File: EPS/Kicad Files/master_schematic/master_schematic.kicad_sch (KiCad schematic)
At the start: 0 parts

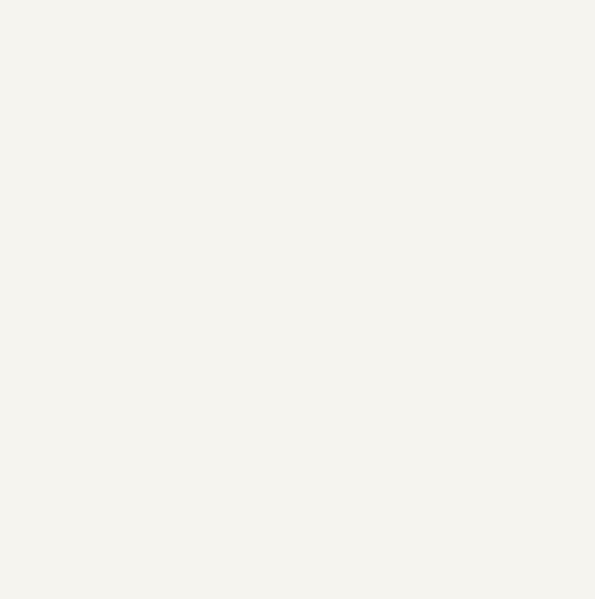
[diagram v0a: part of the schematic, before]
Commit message: Added MCU/CAN to master schematic
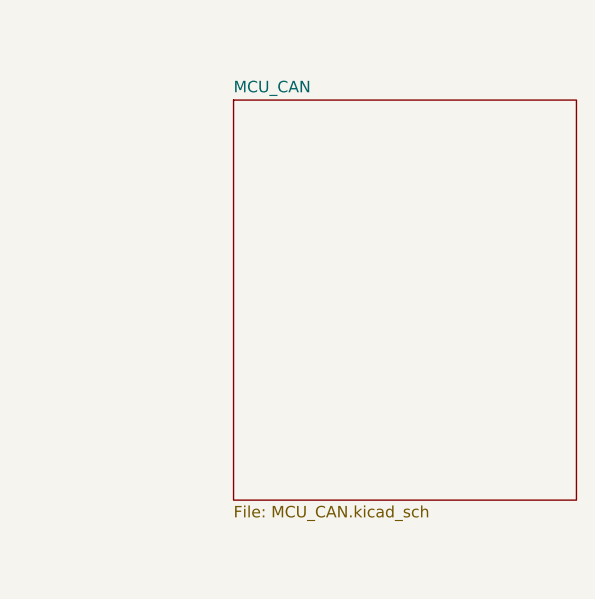
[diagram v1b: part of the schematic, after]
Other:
- added sheet MCU_CAN (MCU_CAN.kicad_sch)
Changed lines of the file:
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@@
+    )
+  )
+  (sheet (at 187.96 67.31) (size 38.1 44.45) (fields_autoplaced)
+    (stroke (width 0.1524) (type solid) (color 0 0 0 0))
+    (fill (color 0 0 0 0.0000))
+    (property "Sheet name" "MCU_CAN" (id 0) (at 187.96 66.5984 0)
+      (effects (font (size 1.27 1.27)) (justify left bottom))
+    )
+    (property "Sheet file" "MCU_CAN.kicad_sch" (id 1) (at 187.96 112.3446 0)
+      (effects (font (size 1.27 1.27)) (justify left top))
     )
   )
@@
     (path "/59a4dc33-016c-4cea-b648-6fe1c8836f68" (page "2"))
     (path "/26a06af6-a463-4c0b-bc99-b7ef2964e4cd" (page "3"))
+    (path "/9fdbccc2-2f8e-4736-8eda-6be5762e5cd4" (page "4"))
   )
   (symbol_instances
@@
       (reference "#PWR01") (unit 1) (value "GNDPWR") (footprint "")
     )
+    (path "/9fdbccc2-2f8e-4736-8eda-6be5762e5cd4/3b6c9550-f562-4564-bb93-fa871679251c"
+      (reference "#PWR0101") (unit 1) (value "+5V") (footprint "")
+    )
     (path "/26a06af6-a463-4c0b-bc99-b7ef2964e4cd/4d6c0c89-4050-4aad-865b-8bf0a01a4f8a"
       (reference "#PWR0101") (unit 1) (value "GND") (footprint "")
     )
+    (path "/9fdbccc2-2f8e-4736-8eda-6be5762e5cd4/5188dfb7-7eb6-4f46-9d1e-d138f6f4b6b9"
+      (reference "#PWR0102") (unit 1) (value "GND") (footprint "")
+    )
     (path "/26a06af6-a463-4c0b-bc99-b7ef2964e4cd/7e8ecf40-acc3-4991-b27f-c274de50e623"
       (reference "#PWR0102") (unit 1) (value "GNDPWR") (footprint "")
     )
+    (path "/9fdbccc2-2f8e-4736-8eda-6be5762e5cd4/938f820b-db08-4a16-82b8-08a6ddecc1d4"
+      (reference "#PWR0103") (unit 1) (value "GND") (footprint "")
+    )
+    (path "/9fdbccc2-2f8e-4736-8eda-6be5762e5cd4/8a5d2036-f5c8-4423-a580-7532d25abfcb"
+      (reference "#PWR0104") (unit 1) (value "+5V") (footprint "")
+    )
     (path "/26a06af6-a463-4c0b-bc99-b7ef2964e4cd/f10741fa-1902-4bc1-9462-3f90d5329911"
       (reference "#PWR0104") (unit 1) (value "GND") (footprint "")
@@
       (reference "#PWR?") (unit 1) (value "GND") (footprint "")
     )
+    (path "/9fdbccc2-2f8e-4736-8eda-6be5762e5cd4/68eca964-9fa2-4a67-b630-c953d1e85d42"
+      (reference "C1") (unit 1) (value "C") (footprint "")
+    )
     (path "/59a4dc33-016c-4cea-b648-6fe1c8836f68/9badf30d-e9b0-4bf0-8024-97ff6edd9f1c"
       (reference "C1") (unit 1) (value "20μF") (footprint "")
@@
       (reference "J1") (unit 1) (value "USB_C_Receptacle") (footprint "Connector_USB:USB_C_Receptacle_Amphenol_12401610E4-2A")
     )
+    (path "/9fdbccc2-2f8e-4736-8eda-6be5762e5cd4/99f4b5e6-a691-4fc9-af7d-e683f2ec248c"
+      (reference "JP1") (unit 1) (value "Jumper_2_Open") (footprint "")
+    )
     (path "/26a06af6-a463-4c0b-bc99-b7ef2964e4cd/3e50bbb4-8a65-44e5-81ec-f7ea9020e1e8"
       (reference "L1") (unit 1) (value ".47uH") (footprint "Inductor_SMD:L_1008_2520Metric")
@@
       (reference "R1") (unit 1) (value "1k") (footprint "Resistor_SMD:R_0402_1005Metric")
     )
+    (path "/9fdbccc2-2f8e-4736-8eda-6be5762e5cd4/ef997102-133d-40f7-998b-a781a8ae245c"
+      (reference "R1") (unit 1) (value "R") (footprint "")
+    )
     (path "/59a4dc33-016c-4cea-b648-6fe1c8836f68/0eedaf4c-41f6-48ba-98ff-d706984035d0"
       (reference "R2") (unit 1) (value "PSF4NTEBL500F") (footprint "footprints:PSF4NTEBL500F")
@@
       (reference "R2") (unit 1) (value "24.9k") (footprint "Resistor_SMD:R_0402_1005Metric")
     )
+    (path "/9fdbccc2-2f8e-4736-8eda-6be5762e5cd4/ff83ad68-5cb3-4e1d-bfd7-46775b78c1ac"
+      (reference "R2") (unit 1) (value "R") (footprint "")
+    )
     (path "/59a4dc33-016c-4cea-b648-6fe1c8836f68/40193638-446d-4ec3-b217-bab5b5e47e99"
       (reference "R3") (unit 1) (value "PSF4NTEBL500F") (footprint "footprints:PSF4NTEBL500F")
@@
       (reference "R3") (unit 1) (value "1k") (footprint "Resistor_SMD:R_0402_1005Metric")
     )
+    (path "/9fdbccc2-2f8e-4736-8eda-6be5762e5cd4/c035cb9d-aa77-4291-97bb-83d02bf9c2a0"
+      (reference "R3") (unit 1) (value "R") (footprint "")
+    )
+    (path "/9fdbccc2-2f8e-4736-8eda-6be5762e5cd4/146d4fbc-56d3-4fb3-82bd-259d588c93f2"
+      (reference "R4") (unit 1) (value "R") (footprint "")
+    )
     (path "/26a06af6-a463-4c0b-bc99-b7ef2964e4cd/7b1c5fbf-250a-41c6-a9a3-633299511edf"
       (reference "R4") (unit 1) (value "10k") (footprint "Resistor_SMD:R_0402_1005Metric")
@@
       (reference "U1") (unit 1) (value "RPM5.0-2.0") (footprint "Converter_DCDC:Converter_DCDC_RECOM_RPMx.x-x.0")
     )
+    (path "/9fdbccc2-2f8e-4736-8eda-6be5762e5cd4/694c3c7b-983e-4abf-8a12-4500e08a960e"
+      (reference "U1") (unit 1) (value "PIC18F27Q84-E/SP") (footprint "PIC18F27Q84-E-SP:PIC18F27Q84-E&slash_SP")
+    )
     (path "/26a06af6-a463-4c0b-bc99-b7ef2964e4cd/921339e0-e2c4-4bf6-a72a-ff2acad226de"
       (reference "U1") (unit 1) (value "MAX77757JEFG435+") (footprint "77757 foot:IC_MAX77757JEFG435+")
     )
+    (path "/9fdbccc2-2f8e-4736-8eda-6be5762e5cd4/1543425c-7d7b-48c0-9e08-4616ac873bc9"
+      (reference "U2") (unit 1) (value "ATA6560-GAQW-VAO") (footprint "ATA6560-GAQW-VAO:ATA6560-GAQW-VAO")
+    )
     (path "/26a06af6-a463-4c0b-bc99-b7ef2964e4cd/62903ce9-1929-4ae0-8378-6aa7c4209eef"

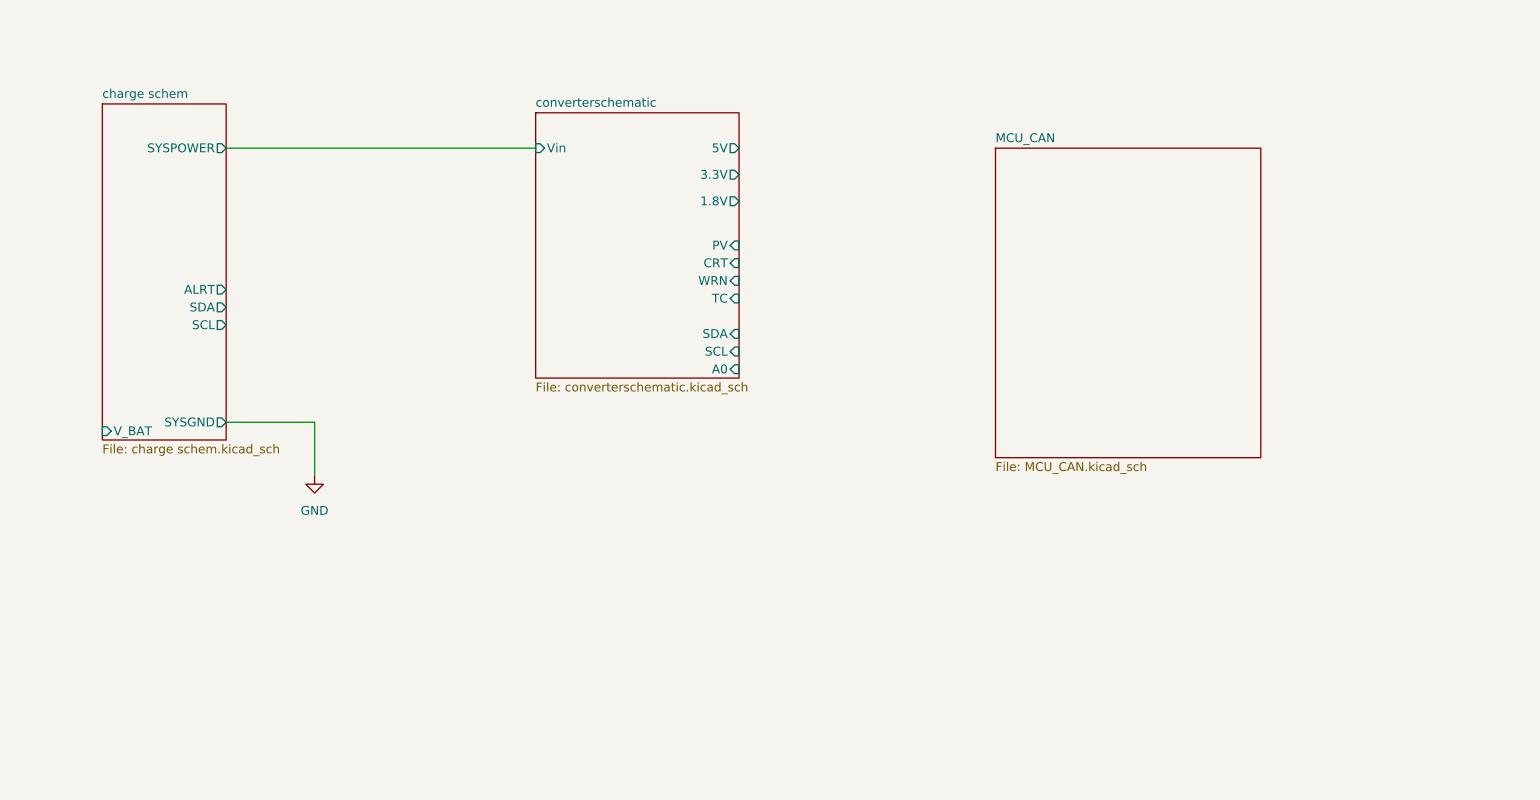
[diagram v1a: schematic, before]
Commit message: master schematic update
added hierarchal pins to MCU_CAN, and attached it with the rest of the circuit
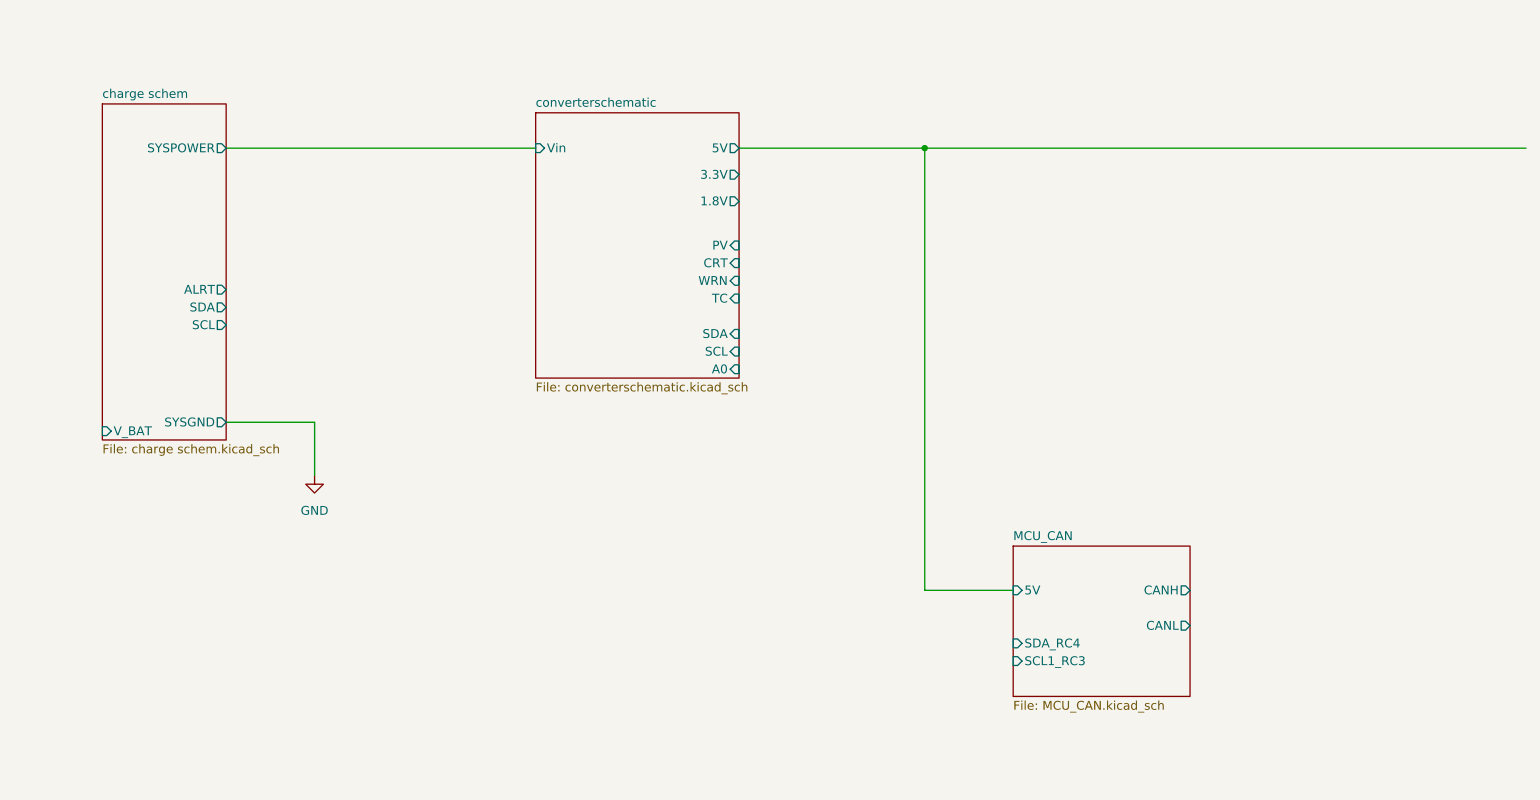
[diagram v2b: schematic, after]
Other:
- sheet MCU_CAN ports: added 5V, CANH, CANL, SCL1_RC3, SDA_RC4; removed none
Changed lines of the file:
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@@
 (kicad_sch (version 20211123) (generator eeschema)
   (paper "A4")
+  (junction (at 177.8 67.31) (diameter 0) (color 0 0 0 0)
+  )
   (wire (pts (xy 77.47 106.68) (xy 90.17 106.68))
     (stroke (width 0) (type default) (color 0 0 0 0))
@@
   )
   (wire (pts (xy 90.17 106.68) (xy 90.17 114.3))
+    (stroke (width 0) (type default) (color 0 0 0 0))
+  )
+  (wire (pts (xy 151.13 67.31) (xy 177.8 67.31))
+    (stroke (width 0) (type default) (color 0 0 0 0))
+  )
+  (wire (pts (xy 177.8 67.31) (xy 264.16 67.31))
+    (stroke (width 0) (type default) (color 0 0 0 0))
+  )
+  (wire (pts (xy 177.8 130.81) (xy 190.5 130.81))
+    (stroke (width 0) (type default) (color 0 0 0 0))
+  )
+  (wire (pts (xy 177.8 67.31) (xy 177.8 130.81))
     (stroke (width 0) (type default) (color 0 0 0 0))
   )
@@
     )
   )
-  (sheet (at 187.96 67.31) (size 38.1 44.45) (fields_autoplaced)
+  (sheet (at 190.5 124.46) (size 25.4 21.59) (fields_autoplaced)
     (stroke (width 0.1524) (type solid) (color 0 0 0 0))
     (fill (color 0 0 0 0.0000))
-    (property "Sheet name" "MCU_CAN" (id 0) (at 187.96 66.5984 0)
+    (property "Sheet name" "MCU_CAN" (id 0) (at 190.5 123.7484 0)
       (effects (font (size 1.27 1.27)) (justify left bottom))
     )
-    (property "Sheet file" "MCU_CAN.kicad_sch" (id 1) (at 187.96 112.3446 0)
+    (property "Sheet file" "MCU_CAN.kicad_sch" (id 1) (at 190.5 146.6346 0)
       (effects (font (size 1.27 1.27)) (justify left top))
+    )
+    (pin "5V" input (at 190.5 130.81 180)
+      (effects (font (size 1.27 1.27)) (justify left))
+    )
+    (pin "CANH" output (at 215.9 130.81 0)
+      (effects (font (size 1.27 1.27)) (justify right))
+    )
+    (pin "CANL" output (at 215.9 135.89 0)
+      (effects (font (size 1.27 1.27)) (justify right))
+    )
+    (pin "SCL1_RC3" input (at 190.5 140.97 180)
+      (effects (font (size 1.27 1.27)) (justify left))
+    )
+    (pin "SDA_RC4" input (at 190.5 138.43 180)
+      (effects (font (size 1.27 1.27)) (justify left))
     )
   )
@@
     (path "/59a4dc33-016c-4cea-b648-6fe1c8836f68" (page "2"))
     (path "/26a06af6-a463-4c0b-bc99-b7ef2964e4cd" (page "3"))
-    (path "/9fdbccc2-2f8e-4736-8eda-6be5762e5cd4" (page "4"))
+    (path "/de6af302-5c4e-471e-a8c4-e4b9e98a4602" (page "5"))
   )
   (symbol_instances
@@
       (reference "#PWR01") (unit 1) (value "GNDPWR") (footprint "")
     )
-    (path "/9fdbccc2-2f8e-4736-8eda-6be5762e5cd4/3b6c9550-f562-4564-bb93-fa871679251c"
-      (reference "#PWR0101") (unit 1) (value "+5V") (footprint "")
-    )
     (path "/26a06af6-a463-4c0b-bc99-b7ef2964e4cd/4d6c0c89-4050-4aad-865b-8bf0a01a4f8a"
       (reference "#PWR0101") (unit 1) (value "GND") (footprint "")
     )
-    (path "/9fdbccc2-2f8e-4736-8eda-6be5762e5cd4/5188dfb7-7eb6-4f46-9d1e-d138f6f4b6b9"
+    (path "/de6af302-5c4e-471e-a8c4-e4b9e98a4602/5188dfb7-7eb6-4f46-9d1e-d138f6f4b6b9"
       (reference "#PWR0102") (unit 1) (value "GND") (footprint "")
     )
@@
       (reference "#PWR0102") (unit 1) (value "GNDPWR") (footprint "")
     )
-    (path "/9fdbccc2-2f8e-4736-8eda-6be5762e5cd4/938f820b-db08-4a16-82b8-08a6ddecc1d4"
+    (path "/de6af302-5c4e-471e-a8c4-e4b9e98a4602/938f820b-db08-4a16-82b8-08a6ddecc1d4"
       (reference "#PWR0103") (unit 1) (value "GND") (footprint "")
-    )
-    (path "/9fdbccc2-2f8e-4736-8eda-6be5762e5cd4/8a5d2036-f5c8-4423-a580-7532d25abfcb"
-      (reference "#PWR0104") (unit 1) (value "+5V") (footprint "")
     )
     (path "/26a06af6-a463-4c0b-bc99-b7ef2964e4cd/f10741fa-1902-4bc1-9462-3f90d5329911"
@@
       (reference "#PWR?") (unit 1) (value "GND") (footprint "")
     )
-    (path "/9fdbccc2-2f8e-4736-8eda-6be5762e5cd4/68eca964-9fa2-4a67-b630-c953d1e85d42"
+    (path "/de6af302-5c4e-471e-a8c4-e4b9e98a4602/68eca964-9fa2-4a67-b630-c953d1e85d42"
       (reference "C1") (unit 1) (value "C") (footprint "")
     )
@@
       (reference "J1") (unit 1) (value "USB_C_Receptacle") (footprint "Connector_USB:USB_C_Receptacle_Amphenol_12401610E4-2A")
     )
-    (path "/9fdbccc2-2f8e-4736-8eda-6be5762e5cd4/99f4b5e6-a691-4fc9-af7d-e683f2ec248c"
+    (path "/de6af302-5c4e-471e-a8c4-e4b9e98a4602/99f4b5e6-a691-4fc9-af7d-e683f2ec248c"
       (reference "JP1") (unit 1) (value "Jumper_2_Open") (footprint "")
     )
@@
       (reference "R1") (unit 1) (value "1k") (footprint "Resistor_SMD:R_0402_1005Metric")
     )
-    (path "/9fdbccc2-2f8e-4736-8eda-6be5762e5cd4/ef997102-133d-40f7-998b-a781a8ae245c"
+    (path "/de6af302-5c4e-471e-a8c4-e4b9e98a4602/ef997102-133d-40f7-998b-a781a8ae245c"
       (reference "R1") (unit 1) (value "R") (footprint "")
     )
@@
       (reference "R2") (unit 1) (value "24.9k") (footprint "Resistor_SMD:R_0402_1005Metric")
     )
-    (path "/9fdbccc2-2f8e-4736-8eda-6be5762e5cd4/ff83ad68-5cb3-4e1d-bfd7-46775b78c1ac"
+    (path "/de6af302-5c4e-471e-a8c4-e4b9e98a4602/ff83ad68-5cb3-4e1d-bfd7-46775b78c1ac"
       (reference "R2") (unit 1) (value "R") (footprint "")
     )
@@
       (reference "R3") (unit 1) (value "1k") (footprint "Resistor_SMD:R_0402_1005Metric")
     )
-    (path "/9fdbccc2-2f8e-4736-8eda-6be5762e5cd4/c035cb9d-aa77-4291-97bb-83d02bf9c2a0"
+    (path "/de6af302-5c4e-471e-a8c4-e4b9e98a4602/c035cb9d-aa77-4291-97bb-83d02bf9c2a0"
       (reference "R3") (unit 1) (value "R") (footprint "")
     )
-    (path "/9fdbccc2-2f8e-4736-8eda-6be5762e5cd4/146d4fbc-56d3-4fb3-82bd-259d588c93f2"
+    (path "/de6af302-5c4e-471e-a8c4-e4b9e98a4602/146d4fbc-56d3-4fb3-82bd-259d588c93f2"
       (reference "R4") (unit 1) (value "R") (footprint "")
     )
@@
       (reference "U1") (unit 1) (value "RPM5.0-2.0") (footprint "Converter_DCDC:Converter_DCDC_RECOM_RPMx.x-x.0")
     )
-    (path "/9fdbccc2-2f8e-4736-8eda-6be5762e5cd4/694c3c7b-983e-4abf-8a12-4500e08a960e"
+    (path "/de6af302-5c4e-471e-a8c4-e4b9e98a4602/694c3c7b-983e-4abf-8a12-4500e08a960e"
       (reference "U1") (unit 1) (value "PIC18F27Q84-E/SP") (footprint "PIC18F27Q84-E-SP:PIC18F27Q84-E&slash_SP")
     )
@@
       (reference "U1") (unit 1) (value "MAX77757JEFG435+") (footprint "77757 foot:IC_MAX77757JEFG435+")
     )
-    (path "/9fdbccc2-2f8e-4736-8eda-6be5762e5cd4/1543425c-7d7b-48c0-9e08-4616ac873bc9"
+    (path "/de6af302-5c4e-471e-a8c4-e4b9e98a4602/1543425c-7d7b-48c0-9e08-4616ac873bc9"
       (reference "U2") (unit 1) (value "ATA6560-GAQW-VAO") (footprint "ATA6560-GAQW-VAO:ATA6560-GAQW-VAO")
     )

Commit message: actual master schematic update
added mcu other files
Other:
- removed sheet MCU_CAN
- added sheet ColoradoCUBE_Payload (ColoradoCUBE_Payload.kicad_sch)
- added sheet Interboard_connector (Interboard_connector.kicad_sch)
